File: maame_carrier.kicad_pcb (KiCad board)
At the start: 2 copper layers, 95 x 116.5 mm, 38 parts, among them J1 To Kakute H7 V1.5: left strip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, J10 FS-iA10B iBUS servo lead (S +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, J11 TF-Luna pin order 1-6 (CFG ti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, J12 Spare FC I2C (5 V supply, sha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, J13 Payload servo power (+ -); se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, J17 Kakute spare: T3 RSSI 3V3(FC)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, J3 VBAT tap from ESC battery pad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, J4 Micro BEC input leads (6-60 V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, J5 Micro BEC output leads (set t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, J6 Spare power: 5V_AUX G 5V_FC G, J7 Pi expansion: 3V3 logic ONLY, J8 TBS M10Q: order matches its p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, J9 SiK radio (UART4), U1 Raspberry Pi Zero W v1.1, com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

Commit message: Fab prep: JLC design rules + Power/VBAT net classes; board nets synced to schematic (0 parity issues); THT headers/Pi socket DNP, wire pads out of BOM; frame holes board-only
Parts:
- F1: value PTC fuse 1812, >=33 V, ~1.1 A hold (part -> PTC fuse 1812, >=33 V, ~1.1 A hold (part TBC)
- J11: value TF-Luna pin order 1-6 (CFG tied to GND = -> TF-Luna pin order 1-6 (CFG tied to GND = I2C mode)
- J8: value TBS M10Q: order matches its pads TX RX G -> TBS M10Q: order matches its pads TX RX GND VCC SCL SDA
- U1: value Raspberry Pi Zero W v1.1, component side -> Raspberry Pi Zero W v1.1, component side up
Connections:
- net 3V3_FC renamed /3V3_FC
- net 3V3_PI renamed /3V3_PI
- net 5V_AUX renamed /5V_AUX
- net 5V_FC renamed /5V_FC
- net BUZZER_SPARE renamed /BUZZER_SPARE
- net GND renamed /GND
- net I2C_SCL renamed /I2C_SCL
- net I2C_SDA renamed /I2C_SDA
- net LED2_A renamed /LED2_A
- net LED3_A renamed /LED3_A
- net LED4_A renamed /LED4_A
- net LED5_A renamed /LED5_A
- net LED6_A renamed /LED6_A
- net LED7_A renamed /LED7_A
- net LED_A renamed /LED_A
- net LED_SPARE renamed /LED_SPARE
- net PI_GPIO12 renamed /PI_GPIO12
- net PI_GPIO13 renamed /PI_GPIO13
- net PI_GPIO17 renamed /PI_GPIO17
- net PI_GPIO22 renamed /PI_GPIO22
- net PI_GPIO23 renamed /PI_GPIO23
- net PI_GPIO24 renamed /PI_GPIO24
- net PI_GPIO25 renamed /PI_GPIO25
- net PI_GPIO26 renamed /PI_GPIO26
- net PI_GPIO27 renamed /PI_GPIO27
- net PI_GPIO4 renamed /PI_GPIO4
- net PI_GPIO5 renamed /PI_GPIO5
- net PI_GPIO6 renamed /PI_GPIO6
- net PI_SCL renamed /PI_SCL
- net PI_SDA renamed /PI_SDA
- net RC_IBUS renamed /RC_IBUS
- net RSSI_SPARE renamed /RSSI_SPARE
- net UART1_FC_RX renamed /UART1_FC_RX
- net UART1_FC_TX renamed /UART1_FC_TX
- net UART3_TX_SPARE renamed /UART3_TX_SPARE
- net UART4_FC_RX renamed /UART4_FC_RX
- net UART4_FC_TX renamed /UART4_FC_TX
- net UART6_FC_RX renamed /UART6_FC_RX
- net UART6_FC_TX renamed /UART6_FC_TX
- net VBAT renamed /VBAT
- net VBAT_F renamed /VBAT_F
- J1 pad 1: (no net) -> unconnected-(J1-B+-Pad1)
- J1 pad 2: (no net) -> unconnected-(J1-Vo-Pad2)
- J1 pad 24: (no net) -> unconnected-(J1-Vi-Pad24)
- J1 pad 25: (no net) -> unconnected-(J1-CAM-Pad25)
- J11 pad 6: (no net) -> unconnected-(J11-MUX-Pad6)
- R3 pad 1: LED_PI_ACTIVE -> /LED_PI_ACTIVE
- R4 pad 1: LED_DATA -> /LED_DATA
- R5 pad 1: LED_BATT_HI -> /LED_BATT_HI
- R6 pad 1: LED_BATT_MID -> /LED_BATT_MID
- R7 pad 1: LED_BATT_LO -> /LED_BATT_LO
- U1 pad 12: (no net) -> /LED_BATT_LO
- U1 pad 19: (no net) -> unconnected-(U1-GPIO10-Pad19)
- U1 pad 21: (no net) -> unconnected-(U1-GPIO9-Pad21)
- U1 pad 23: (no net) -> unconnected-(U1-GPIO11-Pad23)
- U1 pad 24: (no net) -> unconnected-(U1-GPIO8-Pad24)
- U1 pad 26: (no net) -> unconnected-(U1-GPIO7-Pad26)
- U1 pad 27: (no net) -> unconnected-(U1-ID_SD-Pad27)
- U1 pad 28: (no net) -> unconnected-(U1-ID_SC-Pad28)
- U1 pad 35: (no net) -> /LED_BATT_HI
- U1 pad 36: (no net) -> /LED_PI_ACTIVE
- U1 pad 38: (no net) -> /LED_DATA
- U1 pad 40: (no net) -> /LED_BATT_MID

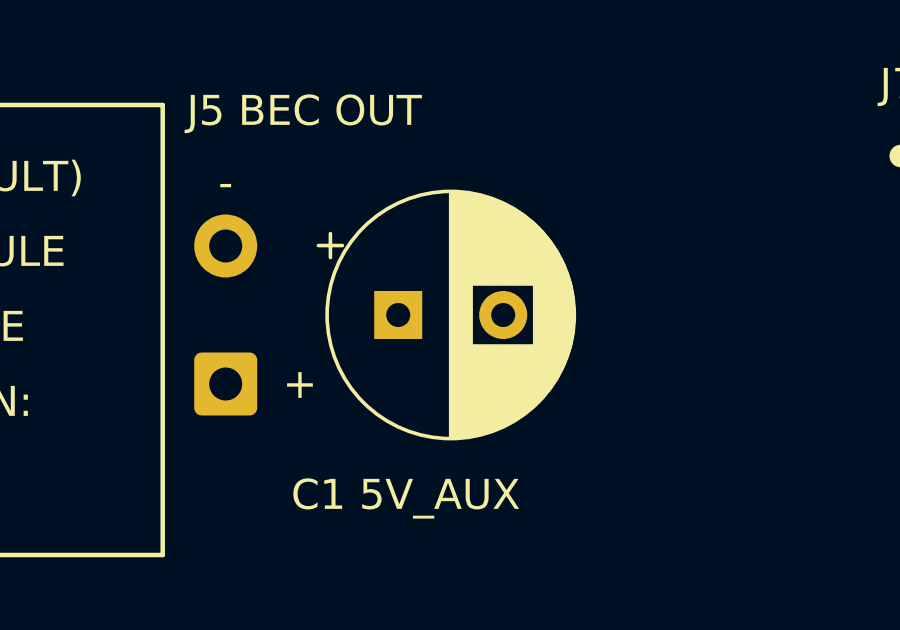
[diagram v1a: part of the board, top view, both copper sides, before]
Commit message: C1 -> SMD 470uF 16V 6.3x7.7 (LCSC C22383803); LCSC fields on all assembled parts
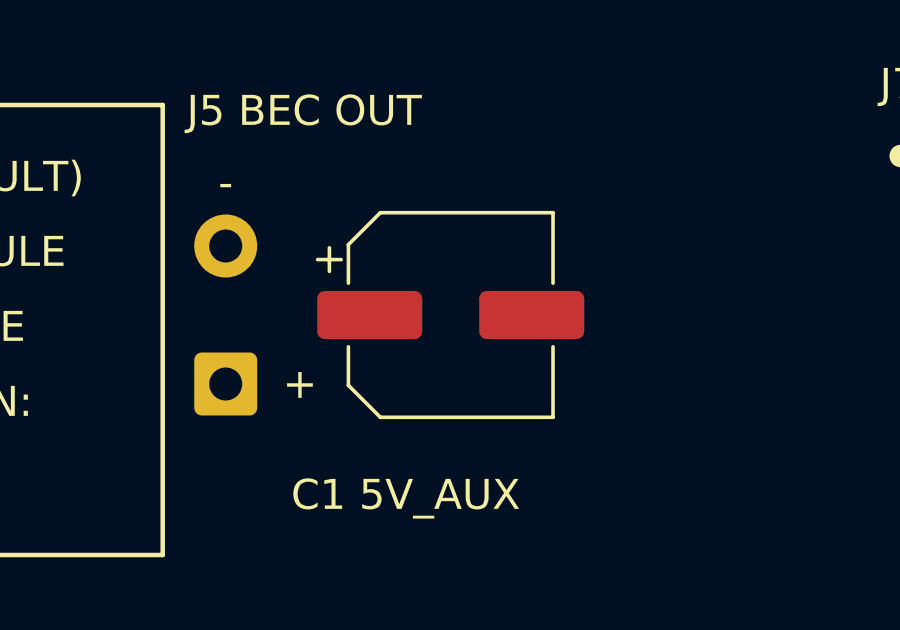
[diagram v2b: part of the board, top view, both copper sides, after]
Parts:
- C1: value 470uF 10V low-ESR (servo/Pi rail) -> 470uF 16V SMD electrolytic (LCSC C22383803); footprint Capacitor_THT:CP_Radial_D8.0mm_P3.50mm -> Capacitor_SMD:CP_Elec_6.3x7.7
- moved C1 1.75 mm to (51.2, 14.1)

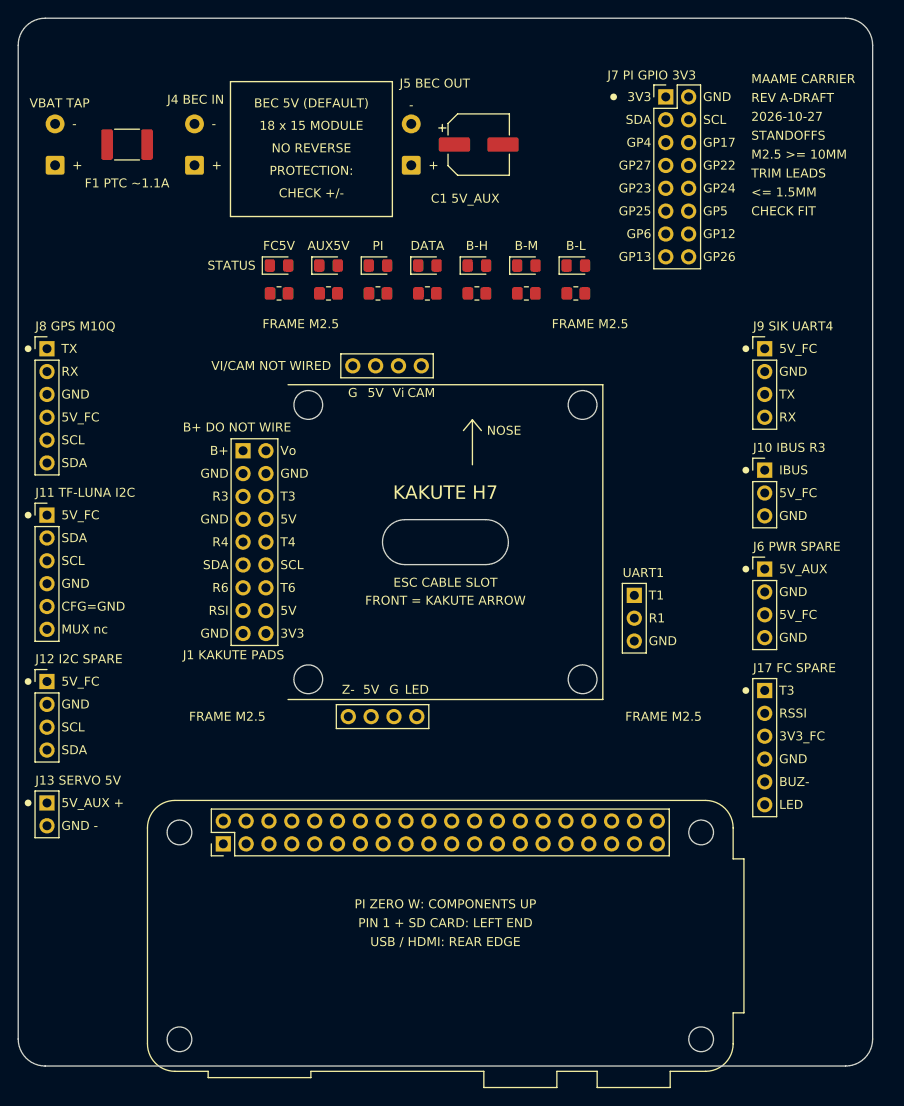
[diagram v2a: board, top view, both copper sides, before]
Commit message: Routed with Freerouting (edge/slot keep-outs, power classes), GND pours both layers with 10 mm stitching; DRC 0 errors, 0 unconnected, parity clean
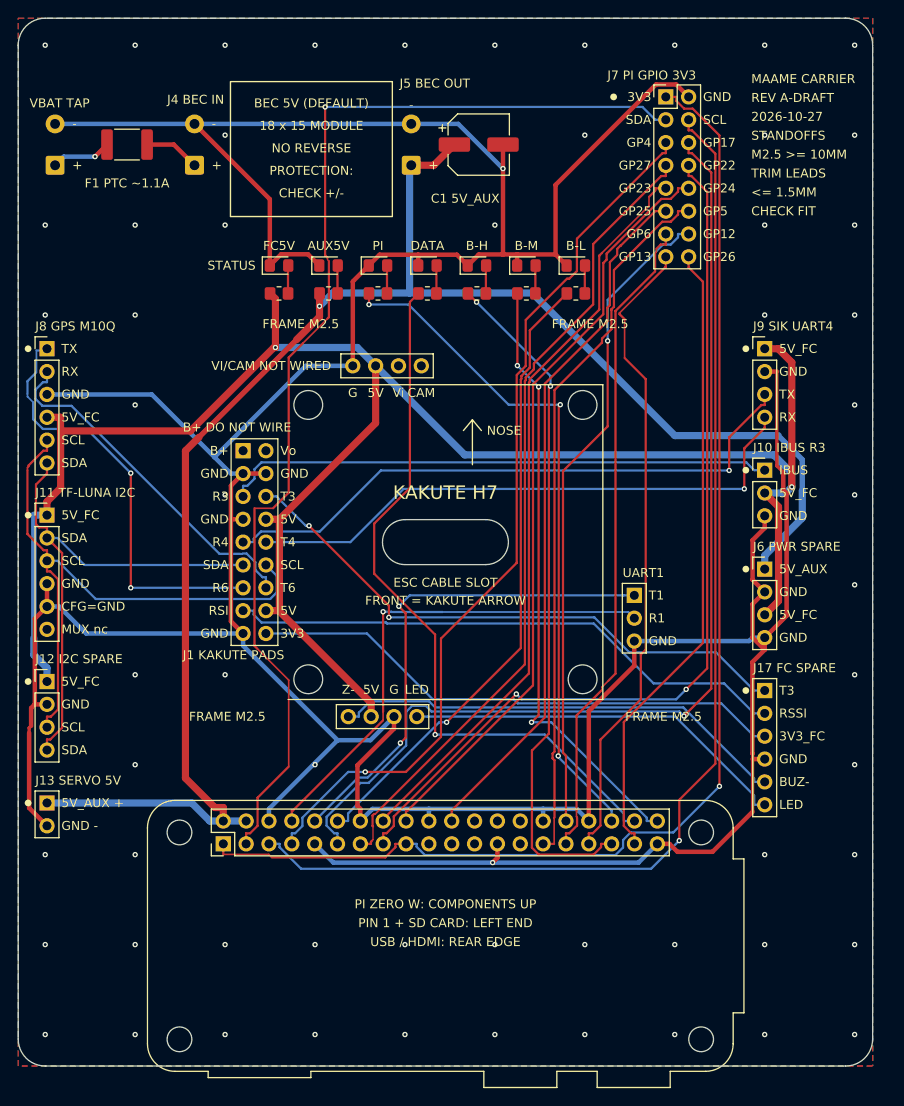
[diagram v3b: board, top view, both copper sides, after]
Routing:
- net /GND: track 0.00 -> 517.5 mm, vias 0 -> 61
- net /5V_FC: track 0.00 -> 218.6 mm, vias 0 -> 2
- net /5V_AUX: track 0.00 -> 186.0 mm, vias 0 -> 1
- net /3V3_PI: track 0.00 -> 142.0 mm, vias 0 -> 1
- net /PI_SCL: track 0.00 -> 131.5 mm, vias 0 -> 1
- net /PI_SDA: track 0.00 -> 129.0 mm, vias 0 -> 1
- net /PI_GPIO17: track 0.00 -> 117.5 mm, vias 0 -> 1
- net /PI_GPIO22: track 0.00 -> 102.9 mm, vias 0 -> 2
- net /PI_GPIO4: track 0.00 -> 99.5 mm, vias 0 -> 1
- net /PI_GPIO27: track 0.00 -> 90.6 mm
- net /PI_GPIO24: track 0.00 -> 84.8 mm
- net /PI_GPIO23: track 0.00 -> 84.1 mm
- net /LED_DATA: track 0.00 -> 80.5 mm, vias 0 -> 1
- net /PI_GPIO5: track 0.00 -> 79.2 mm
- net /PI_GPIO25: track 0.00 -> 78.4 mm
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- added copper zone on B.Cu, net /GND
- added copper zone on F.Cu, net /GND

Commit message: JLCPCB package in fab/: Gerbers + Excellon (zip), BOM and CPL CSVs, top/bottom renders; F1 set to TECHFUSE mSMD110-33V (C70119)
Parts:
- F1: value PTC fuse 1812, >=33 V, ~1.1 A hold (part TBC) -> PTC fuse 1812 33V 1.1A hold (TECHFUSE mSMD110-33V, LCSC C70119)
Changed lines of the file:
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@@
 			)
 		)
-		(property "Value" "PTC fuse 1812, >=33 V, ~1.1 A hold (part TBC)"
+		(property "Value" "PTC fuse 1812 33V 1.1A hold (TECHFUSE mSMD110-33V, LCSC C70119)"
 			(at 0 2.65 0)
 			(layer "F.Fab")

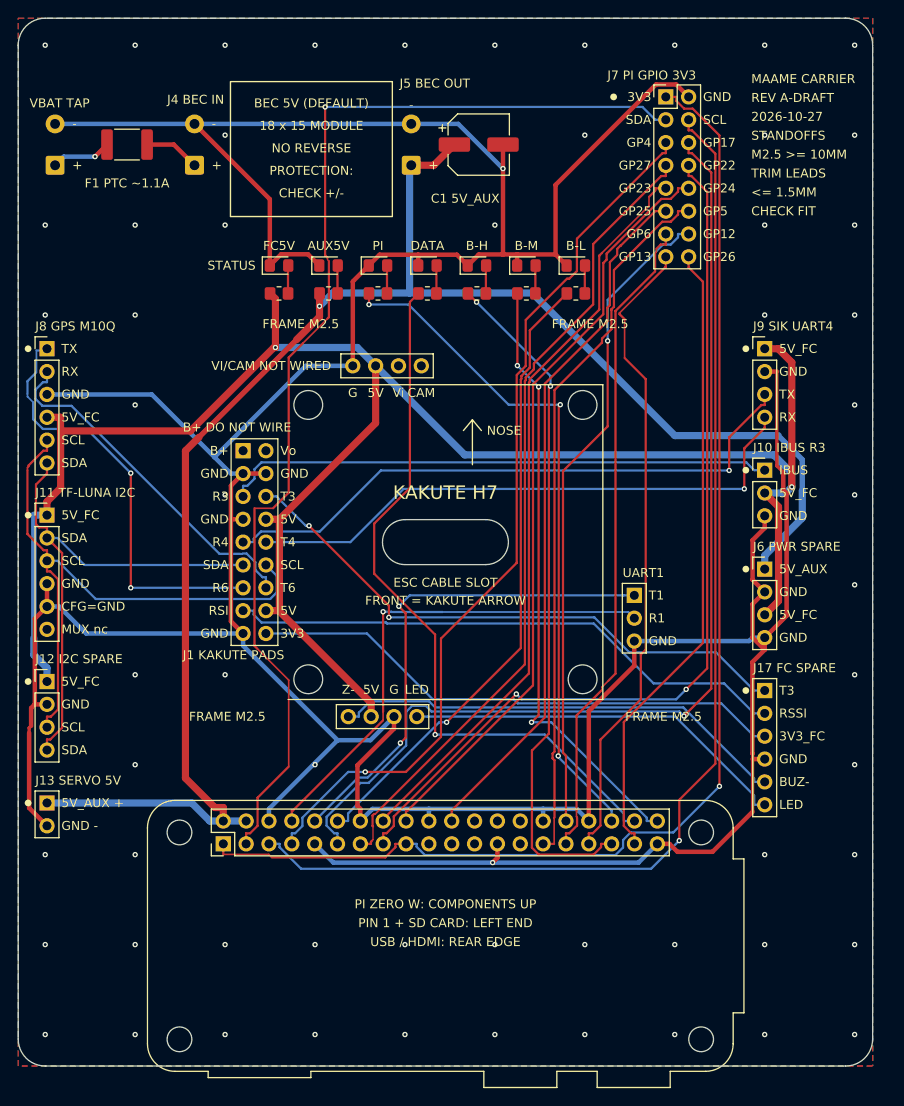
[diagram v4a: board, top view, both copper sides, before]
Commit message: ESC cable slot moved 10.65 mm toward the nose and 3 mm right, under the Kakute ESC connector; re-routed, DRC 0 errors; fab files regenerated
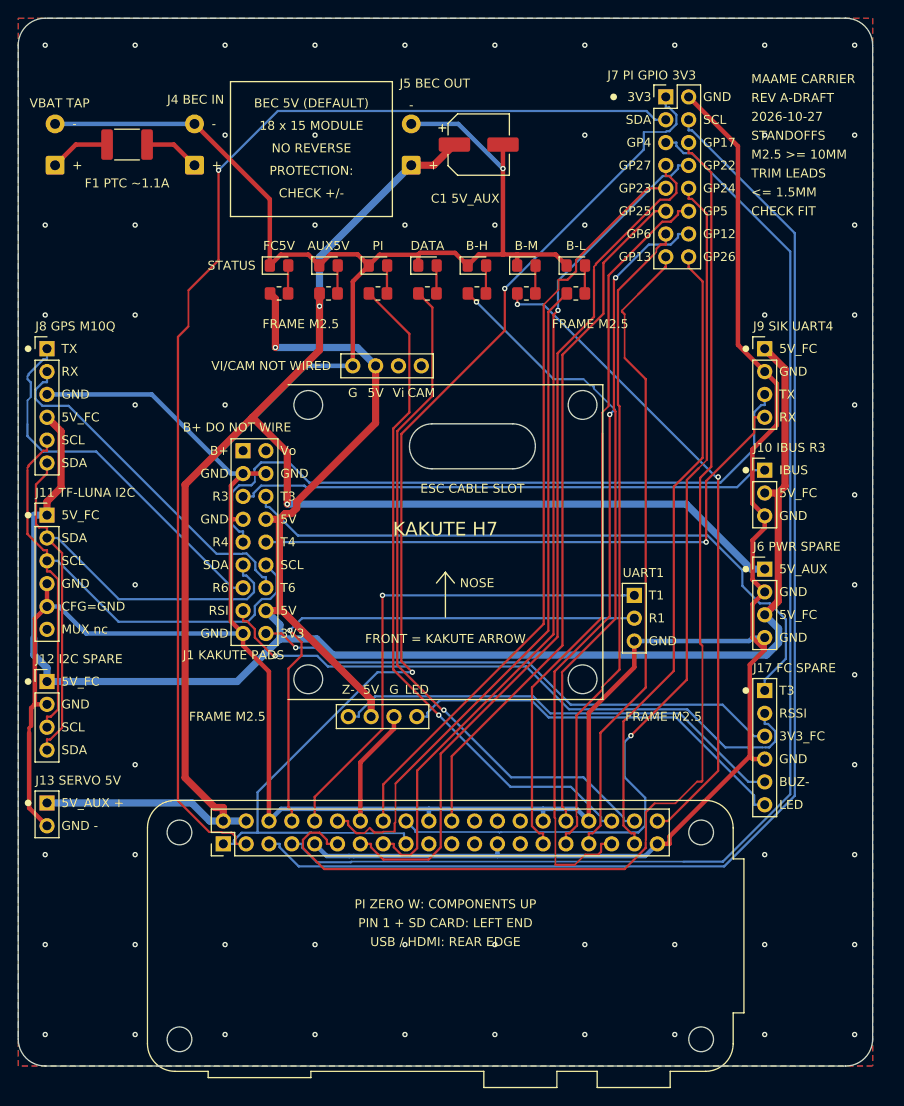
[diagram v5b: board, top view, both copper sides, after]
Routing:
- net /PI_GPIO4: track 99.5 -> 139.1 mm, vias 1 -> 0
- net /GND: track 517.5 -> 484.7 mm, vias 61 -> 60
- net /PI_GPIO24: track 84.8 -> 104.3 mm, vias 0 -> 1
- net /3V3_PI: track 142.0 -> 128.9 mm, vias 1 -> 2
- net /PI_GPIO17: track 117.5 -> 130.5 mm, vias 1 -> 0
- net /PI_SCL: track 131.5 -> 143.2 mm, vias 1 -> 0
- net /UART3_TX_SPARE: track 65.2 -> 74.1 mm, vias 2 -> 0
- net /5V_FC: track 218.6 -> 227.4 mm, vias 2 -> 1
- net /PI_GPIO22: track 102.9 -> 94.5 mm, vias 2 -> 1
- net /UART4_FC_RX: track 67.9 -> 75.9 mm, vias 1 -> 0
- net /PI_GPIO27: track 90.6 -> 98.4 mm
- net /RSSI_SPARE: track 63.0 -> 70.8 mm, vias 0 -> 1
- net /I2C_SDA: track 58.1 -> 65.0 mm
- net /LED_BATT_HI: track 76.2 -> 83.0 mm
- net /UART6_FC_RX: track 48.1 -> 42.1 mm, vias 2 -> 0
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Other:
- outline, holes or cut-outs redrawn

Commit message: 6 mm corner radius; connection legend on the back silkscreen (+ 'LEGEND ON BACK' on top); fab files regenerated
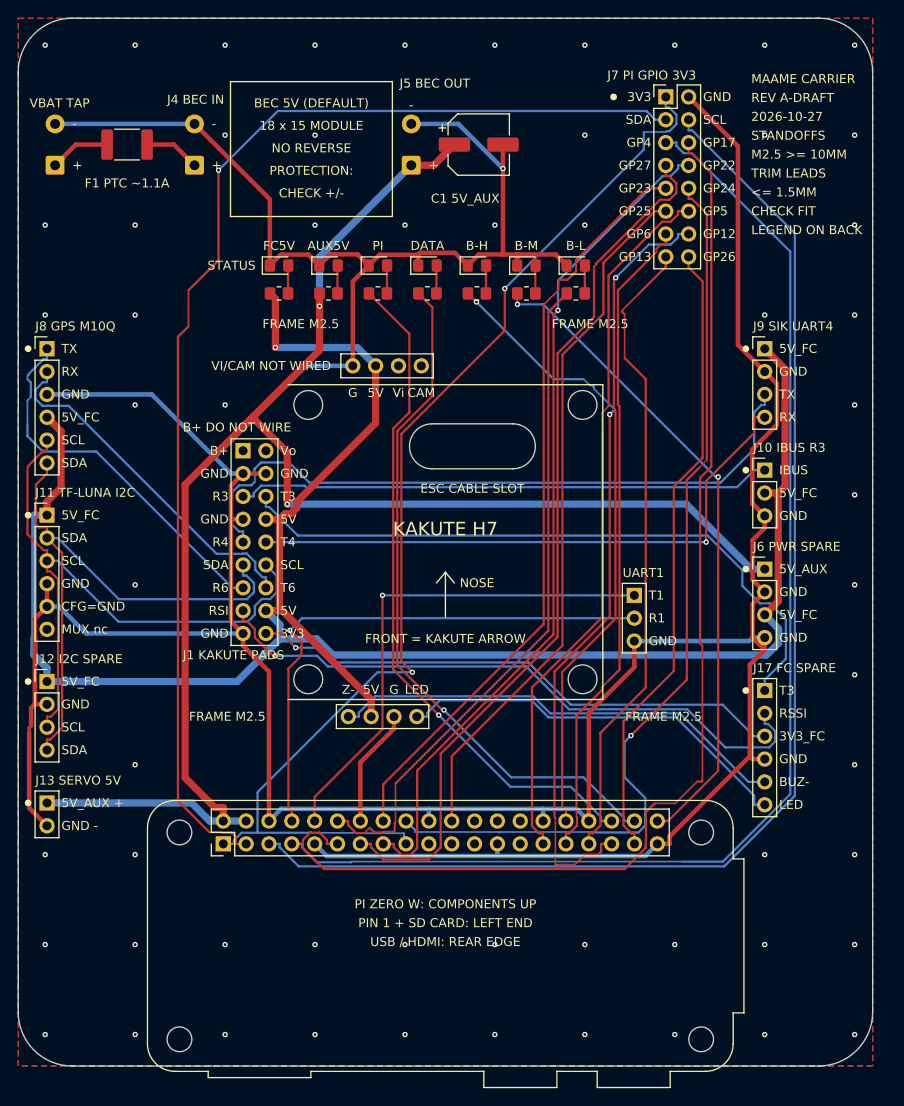
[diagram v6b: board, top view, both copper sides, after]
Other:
- outline, holes or cut-outs redrawn
- board text added: "CONNECTION LEGEND 5V_FC = KAKUTE 5V 5V_AUX = BEC 5V GND COMMON"
- board text added: "J1 KAKUTE PADS 1:1 | T1/R1/G = KAKUTE UART1 TO PI | ESC PORT 1 VIA SLOT"
- board text added: "J11 TF-LUNA I2C | J12 SPARE I2C | J6 SPARE 5V_AUX + 5V_FC"
- board text added: "J13 SERVO 5V_AUX (SIGNAL: KAKUTE M5 PLUG) | J17 T3 RSSI BUZ- LED"
- board text added: "J3 VBAT FROM ESC PADS > F1 > J4 BEC IN | J5 BEC 5V OUT > 5V_AUX"
- board text added: "J7 PI GPIO 3V3 ONLY: I2C + GPIO 4,5,6,12,13,17,22-27"
- board text added: "J8 GPS M10Q UART6+I2C | J9 SIK UART4 | J10 FS-IA10B IBUS > R3"
- board text added: "LEDS: FC5V AUX5V | PI=GPIO16 DATA=GPIO20 | BATT H=19 M=21 L=18"
- board text added: "LEGEND ON BACK"
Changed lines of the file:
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@@
 	)
 	(gr_arc
-		(start 0 3)
-		(mid 0.8787 0.8787)
-		(end 3 0)
+		(start 0 6)
+		(mid 1.7574 1.7574)
+		(end 6 0)
 		(stroke
 			(width 0.05)
@@
 	)
 	(gr_line
-		(start 0 113.5)
-		(end 0 3)
+		(start 0 110.5)
+		(end 0 6)
 		(stroke
 			(width 0.05)
@@
 	)
 	(gr_line
-		(start 3 0)
-		(end 92 0)
+		(start 6 0)
+		(end 89 0)
 		(stroke
 			(width 0.05)
@@
 	)
 	(gr_arc
-		(start 3 116.5)
-		(mid 0.8787 115.621)
-		(end 0 113.5)
+		(start 6 116.5)
+		(mid 1.7574 114.743)
+		(end 0 110.5)
 		(stroke
 			(width 0.05)
@@
 	)
 	(gr_arc
-		(start 92 0)
-		(mid 94.1213 0.8787)
-		(end 95 3)
+		(start 89 0)
+		(mid 93.2426 1.7574)
+		(end 95 6)
 		(stroke
 			(width 0.05)
@@
 	)
 	(gr_line
-		(start 92 116.5)
-		(end 3 116.5)
+		(start 89 116.5)
+		(end 6 116.5)
 		(stroke
 			(width 0.05)
@@
 	)
 	(gr_line
-		(start 95 3)
-		(end 95 113.5)
+		(start 95 6)
+		(end 95 110.5)
 		(stroke
 			(width 0.05)
@@
 	)
 	(gr_arc
-		(start 95 113.5)
-		(mid 94.1213 115.621)
-		(end 92 116.5)
+		(start 95 110.5)
+		(mid 93.2426 114.743)
+		(end 89 116.5)
 		(stroke
 			(width 0.05)
@@
 		)
 	)
+	(gr_text "LEGEND ON BACK"
+		(at 81.5 23.55 0)
+		(layer "F.SilkS")
+		(effects
+			(font
+				(size 1 1)
+				(thickness 0.15)
+			)
+			(justify left)
+		)
+	)
 	(gr_text "CHECK FIT"
 		(at 81.5 21.45 0)
@@
 		)
 	)
+	(gr_text "CONNECTION LEGEND   5V_FC = KAKUTE 5V   5V_AUX = BEC 5V   GND COMMON"
+		(at 47.5 95.6 0)
+		(layer "B.SilkS")
+		(effects
+			(font
+				(size 1 1)
+				(thickness 0.15)
+			)
+			(justify mirror)
+		)
+	)
+	(gr_text "J1 KAKUTE PADS 1:1 | T1/R1/G = KAKUTE UART1 TO PI | ESC PORT 1 VIA SLOT"
+		(at 47.5 97.6 0)
+		(layer "B.SilkS")
+		(effects
+			(font
+				(size 1 1)
+				(thickness 0.15)
+			)
+			(justify mirror)
+		)
+	)
+	(gr_text "J3 VBAT FROM ESC PADS > F1 > J4 BEC IN | J5 BEC 5V OUT > 5V_AUX"
+		(at 47.5 99.6 0)
+		(layer "B.SilkS")
+		(effects
+			(font
+				(size 1 1)
+				(thickness 0.15)
+			)
+			(justify mirror)
+		)
+	)
+	(gr_text "J8 GPS M10Q UART6+I2C | J9 SIK UART4 | J10 FS-IA10B IBUS > R3"
+		(at 47.5 101.6 0)
+		(layer "B.SilkS")
+		(effects
+			(font
+				(size 1 1)
+				(thickness 0.15)
+			)
+			(justify mirror)
+		)
+	)
+	(gr_text "J11 TF-LUNA I2C | J12 SPARE I2C | J6 SPARE 5V_AUX + 5V_FC"
+		(at 47.5 103.6 0)
+		(layer "B.SilkS")
+		(effects
+			(font
+				(size 1 1)
+				(thickness 0.15)
+			)
+			(justify mirror)
+		)
+	)
+	(gr_text "J13 SERVO 5V_AUX (SIGNAL: KAKUTE M5 PLUG) | J17 T3 RSSI BUZ- LED"
+		(at 47.5 105.6 0)
+		(layer "B.SilkS")
+		(effects
+			(font
+				(size 1 1)
+				(thickness 0.15)
+			)
+			(justify mirror)
+		)
+	)
+	(gr_text "J7 PI GPIO 3V3 ONLY: I2C + GPIO 4,5,6,12,13,17,22-27"
+		(at 47.5 107.6 0)
+		(layer "B.SilkS")
+		(effects
+			(font
+				(size 1 1)
+				(thickness 0.15)
+			)
+			(justify mirror)
+		)
+	)
+	(gr_text "LEDS: FC5V AUX5V | PI=GPIO16 DATA=GPIO20 | BATT H=19 M=21 L=18"
+		(at 47.5 109.6 0)
+		(layer "B.SilkS")
+		(effects
+			(font
+				(size 1 1)
+				(thickness 0.15)
+			)
+			(justify mirror)
+		)
+	)
